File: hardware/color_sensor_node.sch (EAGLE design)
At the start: 20 parts, among them J1 JTAG, J2 JTAG, U1 ISL29125, U2 3.3V, U3 WS2811

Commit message: idk
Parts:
- D1: device SparkFun-LED:WS2812B -> SparkFun-LED:WS2812-2020
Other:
- moved on the sheet: C3
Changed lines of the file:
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@@
 <part name="R1" library="SparkFun-Resistors" deviceset="10KOHM" device="-0603-1/10W-1%" value="10k"/>
 <part name="C2" library="SparkFun-Capacitors" deviceset="1.0UF" device="-0603-16V-10%" value="1.0uF"/>
-<part name="D1" library="SparkFun-LED" deviceset="WS2812B" device="" value="WS2812B"/>
+<part name="D1" library="SparkFun-LED" deviceset="WS2812-2020" device="" value="WS2812B"/>
 <part name="U3" library="ws2811" deviceset="WS2811" device=""/>
 <part name="GND5" library="SparkFun-PowerSymbols" deviceset="GND" device=""/>
@@
 <instance part="D1" gate="G$1" x="73.66" y="134.62">
 <attribute name="NAME" x="71.12" y="143.002" size="1.778" layer="95" font="vector" align="bottom-center"/>
-<attribute name="VALUE" x="71.12" y="127" size="1.778" layer="95" font="vector" align="bottom-center"/>
 </instance>
 <instance part="U3" gate="G$1" x="71.12" y="109.22"/>
@@
 <attribute name="VALUE" x="180.34" y="71.374" size="1.778" layer="96" font="vector"/>
 </instance>
-<instance part="C3" gate="G$1" x="48.26" y="88.9">
-<attribute name="NAME" x="49.784" y="91.821" size="1.778" layer="95" font="vector"/>
-<attribute name="VALUE" x="49.784" y="86.741" size="1.778" layer="96" font="vector"/>
+<instance part="C3" gate="G$1" x="48.26" y="86.36">
+<attribute name="NAME" x="49.784" y="89.281" size="1.778" layer="95" font="vector"/>
+<attribute name="VALUE" x="49.784" y="84.201" size="1.778" layer="96" font="vector"/>
 </instance>
 </instances>
@@
 <pinref part="GND4" gate="1" pin="GND"/>
 <pinref part="C3" gate="G$1" pin="2"/>
-<wire x1="48.26" y1="86.36" x2="48.26" y2="81.28" width="0.1524" layer="91"/>
+<wire x1="48.26" y1="83.82" x2="48.26" y2="81.28" width="0.1524" layer="91"/>
 <junction x="48.26" y="81.28"/>
 </segment>
@@
 <wire x1="96.52" y1="96.52" x2="58.42" y2="96.52" width="0.1524" layer="91"/>
 <pinref part="C3" gate="G$1" pin="1"/>
-<wire x1="48.26" y1="96.52" x2="48.26" y2="93.98" width="0.1524" layer="91"/>
+<wire x1="48.26" y1="96.52" x2="48.26" y2="91.44" width="0.1524" layer="91"/>
 <wire x1="58.42" y1="96.52" x2="48.26" y2="96.52" width="0.1524" layer="91"/>
 <junction x="58.42" y="96.52"/>

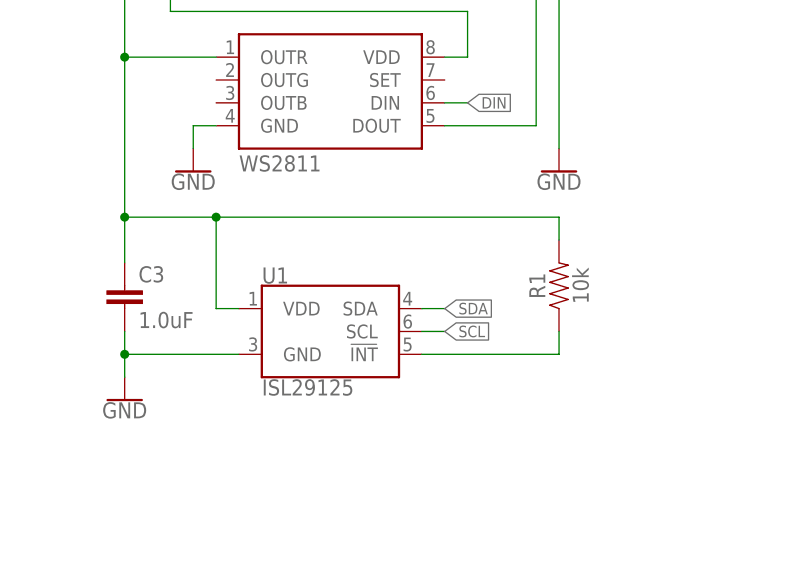
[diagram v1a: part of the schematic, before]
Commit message: reformat sensor board for hook design
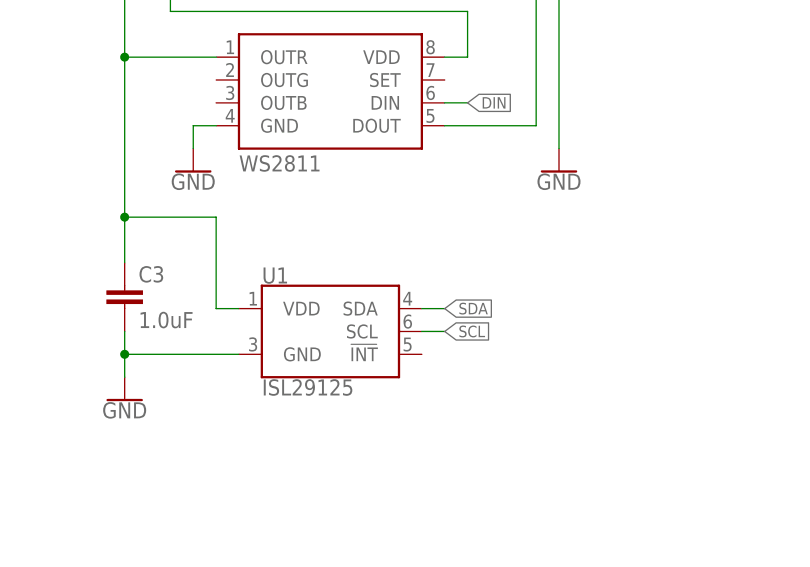
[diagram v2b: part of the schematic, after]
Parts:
- removed R1: 10k, SparkFun-Resistors:10KOHM-0603-1/10W-1%
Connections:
- removed net N$1: R1.1, U1.!INT
- net N$2: no longer R1.2
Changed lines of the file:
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@@
 <part name="GND3" library="SparkFun-PowerSymbols" deviceset="GND" device=""/>
 <part name="GND4" library="SparkFun-PowerSymbols" deviceset="GND" device=""/>
-<part name="R1" library="SparkFun-Resistors" deviceset="10KOHM" device="-0603-1/10W-1%" value="10k"/>
 <part name="C2" library="SparkFun-Capacitors" deviceset="1.0UF" device="-0603-16V-10%" value="1.0uF"/>
 <part name="D1" library="SparkFun-LED" deviceset="WS2812-2020" device="" value="WS2812B"/>
@@
 <attribute name="VALUE" x="48.26" y="75.946" size="1.778" layer="96" align="top-center"/>
 </instance>
-<instance part="R1" gate="G$1" x="96.52" y="88.9" rot="R90">
-<attribute name="NAME" x="94.996" y="88.9" size="1.778" layer="95" font="vector" rot="R90" align="bottom-center"/>
-<attribute name="VALUE" x="98.044" y="88.9" size="1.778" layer="96" font="vector" rot="R90" align="top-center"/>
-</instance>
 <instance part="C2" gate="G$1" x="210.82" y="134.62">
 <attribute name="NAME" x="212.344" y="137.541" size="1.778" layer="95" font="vector"/>
@@
 </segment>
 </net>
-<net name="N$1" class="0">
-<segment>
-<pinref part="U1" gate="G$1" pin="!INT"/>
-<wire x1="81.28" y1="81.28" x2="96.52" y2="81.28" width="0.1524" layer="91"/>
-<pinref part="R1" gate="G$1" pin="1"/>
-<wire x1="96.52" y1="81.28" x2="96.52" y2="83.82" width="0.1524" layer="91"/>
-</segment>
-</net>
 <net name="DIN" class="0">
 <segment>
@@
 <pinref part="R2" gate="G$1" pin="1"/>
 <wire x1="48.26" y1="114.3" x2="48.26" y2="124.46" width="0.1524" layer="91"/>
-<pinref part="R1" gate="G$1" pin="2"/>
-<wire x1="96.52" y1="96.52" x2="96.52" y2="93.98" width="0.1524" layer="91"/>
 <pinref part="U1" gate="G$1" pin="VDD"/>
 <wire x1="58.42" y1="96.52" x2="58.42" y2="86.36" width="0.1524" layer="91"/>
 <wire x1="58.42" y1="86.36" x2="60.96" y2="86.36" width="0.1524" layer="91"/>
-<wire x1="96.52" y1="96.52" x2="58.42" y2="96.52" width="0.1524" layer="91"/>
 <pinref part="C3" gate="G$1" pin="1"/>
 <wire x1="48.26" y1="96.52" x2="48.26" y2="91.44" width="0.1524" layer="91"/>
 <wire x1="58.42" y1="96.52" x2="48.26" y2="96.52" width="0.1524" layer="91"/>
-<junction x="58.42" y="96.52"/>
 <wire x1="48.26" y1="114.3" x2="48.26" y2="96.52" width="0.1524" layer="91"/>
 <junction x="48.26" y="114.3"/>

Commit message: CAM
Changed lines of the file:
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@@
 <?xml version="1.0" encoding="utf-8"?>
 <!DOCTYPE eagle SYSTEM "eagle.dtd">
-<eagle version="9.2.0">
+<eagle version="9.6.0">
 <drawing>
 <settings>
@@
 </plain>
 <instances>
-<instance part="FRAME1" gate="G$1" x="0" y="0"/>
-<instance part="FRAME1" gate="V" x="147.32" y="0">
+<instance part="FRAME1" gate="G$1" x="0" y="0" smashed="yes"/>
+<instance part="FRAME1" gate="V" x="147.32" y="0" smashed="yes">
 <attribute name="LAST_DATE_TIME" x="160.02" y="1.27" size="2.54" layer="94" font="vector"/>
 <attribute name="SHEET" x="233.68" y="1.27" size="2.54" layer="94" font="vector"/>
@@
 <attribute name="REV" x="236.22" y="6.604" size="2.7432" layer="94" font="vector"/>
 </instance>
-<instance part="U1" gate="G$1" x="71.12" y="83.82">
+<instance part="U1" gate="G$1" x="71.12" y="83.82" smashed="yes">
 <attribute name="NAME" x="63.5" y="89.154" size="1.778" layer="95" font="vector"/>
 <attribute name="VALUE" x="63.5" y="78.486" size="1.778" layer="96" font="vector" align="top-left"/>
 </instance>
-<instance part="U2" gate="G$1" x="198.12" y="137.16">
+<instance part="U2" gate="G$1" x="198.12" y="137.16" smashed="yes">
 <attribute name="NAME" x="190.5" y="145.034" size="1.778" layer="95" font="vector"/>
 <attribute name="VALUE" x="190.5" y="129.286" size="1.778" layer="96" font="vector" align="top-left"/>
 </instance>
-<instance part="SUPPLY1" gate="G$1" x="175.26" y="144.78">
+<instance part="SUPPLY1" gate="G$1" x="175.26" y="144.78" smashed="yes">
 <attribute name="VALUE" x="175.26" y="147.574" size="1.778" layer="96" align="bottom-center"/>
 </instance>
-<instance part="SUPPLY2" gate="G$1" x="210.82" y="144.78">
+<instance part="SUPPLY2" gate="G$1" x="210.82" y="144.78" smashed="yes">
 <attribute name="VALUE" x="210.82" y="147.574" size="1.778" layer="96" align="bottom-center"/>
 </instance>
-<instance part="C1" gate="G$1" x="175.26" y="134.62">
+<instance part="C1" gate="G$1" x="175.26" y="134.62" smashed="yes">
 <attribute name="NAME" x="176.784" y="137.541" size="1.778" layer="95" font="vector"/>
 <attribute name="VALUE" x="176.784" y="132.461" size="1.778" layer="96" font="vector"/>
 </instance>
-<instance part="GND1" gate="1" x="185.42" y="127">
+<instance part="GND1" gate="1" x="185.42" y="127" smashed="yes">
 <attribute name="VALUE" x="185.42" y="126.746" size="1.778" layer="96" align="top-center"/>
 </instance>
-<instance part="GND2" gate="1" x="210.82" y="127">
+<instance part="GND2" gate="1" x="210.82" y="127" smashed="yes">
 <attribute name="VALUE" x="210.82" y="126.746" size="1.778" layer="96" align="top-center"/>
 </instance>
-<instance part="GND3" gate="1" x="175.26" y="127">
+<instance part="GND3" gate="1" x="175.26" y="127" smashed="yes">
 <attribute name="VALUE" x="175.26" y="126.746" size="1.778" layer="96" align="top-center"/>
 </instance>
-<instance part="GND4" gate="1" x="48.26" y="76.2">
+<instance part="GND4" gate="1" x="48.26" y="76.2" smashed="yes">
 <attribute name="VALUE" x="48.26" y="75.946" size="1.778" layer="96" align="top-center"/>
 </instance>
-<instance part="C2" gate="G$1" x="210.82" y="134.62">
+<instance part="C2" gate="G$1" x="210.82" y="134.62" smashed="yes">
 <attribute name="NAME" x="212.344" y="137.541" size="1.778" layer="95" font="vector"/>
 <attribute name="VALUE" x="212.344" y="132.461" size="1.778" layer="96" font="vector"/>
 </instance>
-<instance part="D1" gate="G$1" x="73.66" y="134.62">
+<instance part="D1" gate="G$1" x="73.66" y="134.62" smashed="yes">
 <attribute name="NAME" x="71.12" y="143.002" size="1.778" layer="95" font="vector" align="bottom-center"/>
 </instance>
-<instance part="U3" gate="G$1" x="71.12" y="109.22"/>
-<instance part="GND5" gate="1" x="55.88" y="101.6">
+<instance part="U3" gate="G$1" x="71.12" y="109.22" smashed="yes"/>
+<instance part="GND5" gate="1" x="55.88" y="101.6" smashed="yes">
 <attribute name="VALUE" x="55.88" y="101.346" size="1.778" layer="96" align="top-center"/>
 </instance>
-<instance part="SUPPLY6" gate="G$1" x="53.34" y="142.24">
+<instance part="SUPPLY6" gate="G$1" x="53.34" y="142.24" smashed="yes">
 <attribute name="VALUE" x="53.34" y="145.034" size="1.778" layer="96" align="bottom-center"/>
 </instance>
-<instance part="GND6" gate="1" x="96.52" y="101.6">
+<instance part="GND6" gate="1" x="96.52" y="101.6" smashed="yes">
 <attribute name="VALUE" x="96.52" y="101.346" size="1.778" layer="96" align="top-center"/>
 </instance>
-<instance part="SUPPLY3" gate="G$1" x="48.26" y="142.24">
+<instance part="SUPPLY3" gate="G$1" x="48.26" y="142.24" smashed="yes">
 <attribute name="VALUE" x="48.26" y="145.034" size="1.778" layer="96" align="bottom-center"/>
 </instance>
-<instance part="R2" gate="G$1" x="48.26" y="129.54" rot="R90">
+<instance part="R2" gate="G$1" x="48.26" y="129.54" smashed="yes" rot="R90">
 <attribute name="NAME" x="46.736" y="129.54" size="1.778" layer="95" font="vector" rot="R90" align="bottom-center"/>
 <attribute name="VALUE" x="49.784" y="129.54" size="1.778" layer="96" font="vector" rot="R90" align="top-center"/>
 </instance>
-<instance part="SUPPLY8" gate="G$1" x="213.36" y="111.76">
+<instance part="SUPPLY8" gate="G$1" x="213.36" y="111.76" smashed="yes">
 <attribute name="VALUE" x="213.36" y="114.554" size="1.778" layer="96" align="bottom-center"/>
 </instance>
-<instance part="SUPPLY9" gate="G$1" x="213.36" y="86.36">
+<instance part="SUPPLY9" gate="G$1" x="213.36" y="86.36" smashed="yes">
 <attribute name="VALUE" x="213.36" y="89.154" size="1.778" layer="96" align="bottom-center"/>
 </instance>
-<instance part="GND8" gate="1" x="210.82" y="96.52">
+<instance part="GND8" gate="1" x="210.82" y="96.52" smashed="yes">
 <attribute name="VALUE" x="210.82" y="96.266" size="1.778" layer="96" align="top-center"/>
 </instance>
-<instance part="GND9" gate="1" x="210.82" y="71.12">
+<instance part="GND9" gate="1" x="210.82" y="71.12" smashed="yes">
 <attribute name="VALUE" x="210.82" y="70.866" size="1.778" layer="96" align="top-center"/>
 </instance>
-<instance part="H1" gate="G$1" x="223.52" y="33.02"/>
-<instance part="H2" gate="G$1" x="226.06" y="33.02"/>
-<instance part="H3" gate="G$1" x="226.06" y="30.48"/>
-<instance part="H4" gate="G$1" x="223.52" y="30.48"/>
-<instance part="FD1" gate="G$1" x="231.14" y="33.02"/>
-<instance part="FD2" gate="G$1" x="231.14" y="30.48"/>
-<instance part="FD3" gate="G$1" x="233.68" y="30.48"/>
-<instance part="FD4" gate="G$1" x="233.68" y="33.02"/>
-<instance part="GND7" gate="1" x="175.26" y="96.52">
+<instance part="H1" gate="G$1" x="223.52" y="33.02" smashed="yes"/>
+<instance part="H2" gate="G$1" x="226.06" y="33.02" smashed="yes"/>
+<instance part="H3" gate="G$1" x="226.06" y="30.48" smashed="yes"/>
+<instance part="H4" gate="G$1" x="223.52" y="30.48" smashed="yes"/>
+<instance part="FD1" gate="G$1" x="231.14" y="33.02" smashed="yes"/>
+<instance part="FD2" gate="G$1" x="231.14" y="30.48" smashed="yes"/>
+<instance part="FD3" gate="G$1" x="233.68" y="30.48" smashed="yes"/>
+<instance part="FD4" gate="G$1" x="233.68" y="33.02" smashed="yes"/>
+<instance part="GND7" gate="1" x="175.26" y="96.52" smashed="yes">
 <attribute name="VALUE" x="175.26" y="96.266" size="1.778" layer="96" align="top-center"/>
 </instance>
-<instance part="SUPPLY7" gate="G$1" x="172.72" y="111.76">
+<instance part="SUPPLY7" gate="G$1" x="172.72" y="111.76" smashed="yes">
 <attribute name="VALUE" x="172.72" y="114.554" size="1.778" layer="96" align="bottom-center"/>
 </instance>
-<instance part="GND10" gate="1" x="175.26" y="71.12">
+<instance part="GND10" gate="1" x="175.26" y="71.12" smashed="yes">
 <attribute name="VALUE" x="175.26" y="70.866" size="1.778" layer="96" align="top-center"/>
 </instance>
-<instance part="SUPPLY10" gate="G$1" x="172.72" y="86.36">
+<instance part="SUPPLY10" gate="G$1" x="172.72" y="86.36" smashed="yes">
 <attribute name="VALUE" x="172.72" y="89.154" size="1.778" layer="96" align="bottom-center"/>
 </instance>
-<instance part="J1" gate="J1" x="193.04" y="106.68">
+<instance part="J1" gate="J1" x="193.04" y="106.68" smashed="yes">
 <attribute name="NAME" x="180.34" y="114.554" size="1.778" layer="95" font="vector"/>
 <attribute name="VALUE" x="180.34" y="96.774" size="1.778" layer="96" font="vector"/>
 </instance>
-<instance part="J2" gate="J1" x="193.04" y="81.28">
+<instance part="J2" gate="J1" x="193.04" y="81.28" smashed="yes">
 <attribute name="NAME" x="180.34" y="89.154" size="1.778" layer="95" font="vector"/>
 <attribute name="VALUE" x="180.34" y="71.374" size="1.778" layer="96" font="vector"/>
 </instance>
-<instance part="C3" gate="G$1" x="48.26" y="86.36">
+<instance part="C3" gate="G$1" x="48.26" y="86.36" smashed="yes">
 <attribute name="NAME" x="49.784" y="89.281" size="1.778" layer="95" font="vector"/>
 <attribute name="VALUE" x="49.784" y="84.201" size="1.778" layer="96" font="vector"/>
